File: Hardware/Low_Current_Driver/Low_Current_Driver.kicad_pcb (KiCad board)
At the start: 4 copper layers, 0 parts

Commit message: Checkpoint before channel-replication refactor
Snapshot of schematic/PCB work-in-progress prior to restructuring
Channel_Outputs into a reusable hierarchical channel sheet for
replicate-layout. Adds DPST relay footprint.

Co-Authored-By: Claude Opus 4.8 <noreply@anthropic.com>
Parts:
- added A1: Arduino_Nano_Every, Module:Arduino_Nano, F.Cu at (187.5, 108.2)
- added C10: 10n, Capacitor_SMD:C_0603_1608Metric_Pad1.08x0.95mm_HandSolder, F.Cu at (154.7, 98.2)
- added C11: 47u, Capacitor_SMD:C_1210_3225Metric_Pad1.33x2.70mm_HandSolder, F.Cu at (154.9, 76.2)
- added C12: 47u, Capacitor_SMD:C_1210_3225Metric_Pad1.33x2.70mm_HandSolder, F.Cu at (155.9, 86.2)
- added C13: 47u, Capacitor_SMD:C_1210_3225Metric_Pad1.33x2.70mm_HandSolder, F.Cu at (161.9, 97.3)
- added C14: 100n, Capacitor_SMD:C_0603_1608Metric_Pad1.08x0.95mm_HandSolder, F.Cu at (196.3, 70.2)
- added C15: 100n, Capacitor_SMD:C_0603_1608Metric_Pad1.08x0.95mm_HandSolder, F.Cu at (223.3, 78.2)
- added C16: 100n, Capacitor_SMD:C_0603_1608Metric_Pad1.08x0.95mm_HandSolder, F.Cu at (214.4, 88.2)
- added C17: 100n, Capacitor_SMD:C_0603_1608Metric_Pad1.08x0.95mm_HandSolder, F.Cu at (219.8, 89.7)
- added C18: 100n, Capacitor_SMD:C_0603_1608Metric_Pad1.08x0.95mm_HandSolder, F.Cu at (212.3, 103.2)
- added C21: 1u, Capacitor_SMD:C_0603_1608Metric_Pad1.08x0.95mm_HandSolder, F.Cu at (223.4, 80.2)
- added C22: 1u, Capacitor_SMD:C_0603_1608Metric_Pad1.08x0.95mm_HandSolder, F.Cu at (214.4, 90.7)
- added C23: 47u, Capacitor_SMD:C_1210_3225Metric_Pad1.33x2.70mm_HandSolder, F.Cu at (203.2, 80.6)
- added C24: 1u, Capacitor_SMD:C_0603_1608Metric_Pad1.08x0.95mm_HandSolder, F.Cu at (219.8, 92.2)
- added C25: 1u, Capacitor_SMD:C_0603_1608Metric_Pad1.08x0.95mm_HandSolder, F.Cu at (212.1, 100.6)
- added C28: 10u, Capacitor_SMD:C_1206_3216Metric_Pad1.33x1.80mm_HandSolder, F.Cu at (203.2, 76.8)
- added C29: 10n, Capacitor_SMD:C_0603_1608Metric_Pad1.08x0.95mm_HandSolder, F.Cu at (209.8, 89.1)
- added C30: 100n, Capacitor_SMD:C_0603_1608Metric_Pad1.08x0.95mm_HandSolder, F.Cu at (209.8, 91.2)
- added C34: 100n, Capacitor_SMD:C_0603_1608Metric_Pad1.08x0.95mm_HandSolder, F.Cu at (223.9, 96.2)
- added C35: 100n, Capacitor_SMD:C_0603_1608Metric_Pad1.08x0.95mm_HandSolder, F.Cu at (228.4, 84.7)
- added C37: 100n, Capacitor_SMD:C_0603_1608Metric_Pad1.08x0.95mm_HandSolder, F.Cu at (253.9, 93.7)
- added C38: 100n, Capacitor_SMD:C_0603_1608Metric_Pad1.08x0.95mm_HandSolder, F.Cu at (246.4, 102.7)
- added C39: 100n, Capacitor_SMD:C_0603_1608Metric_Pad1.08x0.95mm_HandSolder, F.Cu at (268.0, 87.1)
- added C4: 10u, Capacitor_SMD:C_1206_3216Metric_Pad1.33x1.80mm_HandSolder, F.Cu at (144.7, 73.7)
- added C40: 100n, Capacitor_SMD:C_0603_1608Metric_Pad1.08x0.95mm_HandSolder, F.Cu at (268.0, 89.6)
- added C49: 1u, Capacitor_SMD:C_0603_1608Metric_Pad1.08x0.95mm_HandSolder, F.Cu at (243.9, 99.7)
- added C5: 10u, Capacitor_SMD:C_1206_3216Metric_Pad1.33x1.80mm_HandSolder, F.Cu at (144.7, 87.7)
- added C50: 1u, Capacitor_SMD:C_0603_1608Metric_Pad1.08x0.95mm_HandSolder, F.Cu at (240.8, 75.9)
- added C52: 1u, Capacitor_SMD:C_0603_1608Metric_Pad1.08x0.95mm_HandSolder, F.Cu at (246.9, 94.2)
- added C53: 1u, Capacitor_SMD:C_0603_1608Metric_Pad1.08x0.95mm_HandSolder, F.Cu at (240.8, 80.9)
- added C54: 4.7u, Capacitor_SMD:C_0603_1608Metric_Pad1.08x0.95mm_HandSolder, F.Cu at (238.9, 102.7)
- added C55: 4.7u, Capacitor_SMD:C_0603_1608Metric_Pad1.08x0.95mm_HandSolder, F.Cu at (245.1, 65.8)
- added C6: 10u, Capacitor_SMD:C_1206_3216Metric_Pad1.33x1.80mm_HandSolder, F.Cu at (145.9, 103.2)
- added C7: 1u, Capacitor_SMD:C_0603_1608Metric_Pad1.08x0.95mm_HandSolder, F.Cu at (144.7, 79.2)
- added C8: 1u, Capacitor_SMD:C_0603_1608Metric_Pad1.08x0.95mm_HandSolder, F.Cu at (149.4, 83.2)
- added C9: 1u, Capacitor_SMD:C_0603_1608Metric_Pad1.08x0.95mm_HandSolder, F.Cu at (144.9, 97.3)
- added J1: Conn_01x02_Socket, Connector_Molex:Molex_Micro-Fit_3.0_43650-0215_1x02_P3.00mm_Vertical, F.Cu at (307.4, 84.3)
- added J2: Conn_01x02_Socket, Connector_Molex:Molex_Micro-Fit_3.0_43650-0215_1x02_P3.00mm_Vertical, F.Cu at (307.4, 92.1)
- added J3: Screw_Terminal_01x04, TerminalBlock_Phoenix:TerminalBlock_Phoenix_MKDS-1,5-4-5.08_1x04_P5.08mm_Horizontal, F.Cu at (110.2, 80.0)
- added NT1: Net-Tie_3, NetTie:NetTie-3_SMD_Pad2.0mm, F.Cu at (214.4, 47.6)
- added R13: 549k, Resistor_SMD:R_0603_1608Metric_Pad0.98x0.95mm_HandSolder, F.Cu at (157.9, 98.2)
- added R14: 102k, Resistor_SMD:R_0603_1608Metric_Pad0.98x0.95mm_HandSolder, F.Cu at (157.9, 94.1)
- added R18: 10k, Resistor_SMD:R_0603_1608Metric_Pad0.98x0.95mm_HandSolder, F.Cu at (200.9, 98.2)
- added R19: 10k, Resistor_SMD:R_0603_1608Metric_Pad0.98x0.95mm_HandSolder, F.Cu at (202.9, 98.2)
- added R20: 10k, Resistor_SMD:R_0603_1608Metric_Pad0.98x0.95mm_HandSolder, F.Cu at (221.4, 100.3)
- added R21: 10k, Resistor_SMD:R_0603_1608Metric_Pad0.98x0.95mm_HandSolder, F.Cu at (208.4, 93.8)
- added R22: 10k, Resistor_SMD:R_0603_1608Metric_Pad0.98x0.95mm_HandSolder, F.Cu at (210.4, 94.2)
- added R23: 10k, Resistor_SMD:R_0603_1608Metric_Pad0.98x0.95mm_HandSolder, F.Cu at (225.4, 88.7)
- added R24: 10k, Resistor_SMD:R_0603_1608Metric_Pad0.98x0.95mm_HandSolder, F.Cu at (211.4, 82.2)
- added R25: 10k, Resistor_SMD:R_0603_1608Metric_Pad0.98x0.95mm_HandSolder, F.Cu at (213.4, 82.2)
- added R29: 10k, Resistor_SMD:R_0603_1608Metric_Pad0.98x0.95mm_HandSolder, F.Cu at (221.4, 96.3)
- added R30: 10k, Resistor_SMD:R_0603_1608Metric_Pad0.98x0.95mm_HandSolder, F.Cu at (225.4, 84.7)
- added R32: 1k, Resistor_SMD:R_0603_1608Metric_Pad0.98x0.95mm_HandSolder, F.Cu at (240.4, 96.7)
- added R33: 1k, Resistor_SMD:R_0603_1608Metric_Pad0.98x0.95mm_HandSolder, F.Cu at (245.1, 70.9)
- added R35: 1k, Resistor_SMD:R_0603_1608Metric_Pad0.98x0.95mm_HandSolder, F.Cu at (244.9, 96.7)
- added R36: 1k, Resistor_SMD:R_0603_1608Metric_Pad0.98x0.95mm_HandSolder, F.Cu at (245.1, 75.9)
- added R38: 1k, Resistor_SMD:R_0603_1608Metric_Pad0.98x0.95mm_HandSolder, F.Cu at (257.4, 102.1)
- added R39: 249, Resistor_SMD:R_0603_1608Metric_Pad0.98x0.95mm_HandSolder, F.Cu at (249.5, 103.7)
- added R40: 1k, Resistor_SMD:R_0603_1608Metric_Pad0.98x0.95mm_HandSolder, F.Cu at (249.5, 63.3)
- added R41: 249, Resistor_SMD:R_0603_1608Metric_Pad0.98x0.95mm_HandSolder, F.Cu at (249.5, 65.8)
- added R44: 1k, Resistor_SMD:R_0603_1608Metric_Pad0.98x0.95mm_HandSolder, F.Cu at (257.4, 98.0)
- added R45: 1k, Resistor_SMD:R_0603_1608Metric_Pad0.98x0.95mm_HandSolder, F.Cu at (253.4, 103.7)
- added R46: 1k, Resistor_SMD:R_0603_1608Metric_Pad0.98x0.95mm_HandSolder, F.Cu at (249.5, 73.4)
- added R47: 1k, Resistor_SMD:R_0603_1608Metric_Pad0.98x0.95mm_HandSolder, F.Cu at (249.5, 75.9)
- added SW1: SW_DPST, fieldZero:DPST_RA83231100, F.Cu at (129.3, 87.6)
- added TP1: TestPoint_Probe, TestPoint:TestPoint_Pad_D1.0mm, F.Cu at (134.4, 77.6)
- added TP12: TestPoint_Probe, TestPoint:TestPoint_Pad_D1.0mm, F.Cu at (154.4, 90.2)
- added TP13: TestPoint_Probe, TestPoint:TestPoint_Pad_D1.0mm, F.Cu at (154.9, 102.7)
- added TP14: TestPoint_Probe, TestPoint:TestPoint_Pad_D1.0mm, F.Cu at (154.9, 80.2)
- added TP15: TestPoint_Probe, TestPoint:TestPoint_Pad_D1.0mm, F.Cu at (203.9, 68.1)
- added TP16: TestPoint_Probe, TestPoint:TestPoint_Pad_D1.0mm, F.Cu at (203.9, 71.2)
- added TP17: TestPoint_Probe, TestPoint:TestPoint_Pad_D1.0mm, F.Cu at (218.8, 124.7)
- added TP18: TestPoint_Probe, TestPoint:TestPoint_Pad_D1.0mm, F.Cu at (221.9, 118.6)
- added TP19: TestPoint_Probe, TestPoint:TestPoint_Pad_D1.0mm, F.Cu at (221.9, 121.7)
- added TP2: TestPoint_Probe, TestPoint:TestPoint_Pad_D1.0mm, F.Cu at (134.4, 97.6)
- added TP20: TestPoint_Probe, TestPoint:TestPoint_Pad_D1.0mm, F.Cu at (221.9, 124.7)
- added TP21: TestPoint_Probe, TestPoint:TestPoint_Pad_D1.0mm, F.Cu at (224.9, 118.6)
- added TP23: TestPoint_Probe, TestPoint:TestPoint_Pad_D1.0mm, F.Cu at (83.4, 53.5)
- added TP24: TestPoint_Probe, TestPoint:TestPoint_Pad_D1.0mm, F.Cu at (83.4, 56.6)
- added TP25: TestPoint_Probe, TestPoint:TestPoint_Pad_D1.0mm, F.Cu at (83.4, 59.6)
- added TP26: TestPoint_Probe, TestPoint:TestPoint_Pad_D1.0mm, F.Cu at (83.4, 62.7)
- added TP27: TestPoint_Probe, TestPoint:TestPoint_Pad_D1.0mm, F.Cu at (86.5, 53.5)
- added TP28: TestPoint_Probe, TestPoint:TestPoint_Pad_D1.0mm, F.Cu at (86.5, 56.6)
- added TP30: TestPoint_Probe, TestPoint:TestPoint_Pad_D1.0mm, F.Cu at (133.9, 115.7)
- added TP31: TestPoint_Probe, TestPoint:TestPoint_Pad_D1.0mm, F.Cu at (264.4, 125.6)
- added TP32: TestPoint_Probe, TestPoint:TestPoint_Pad_D1.0mm, F.Cu at (253.2, 79.8)
- added TP33: TestPoint_Probe, TestPoint:TestPoint_Pad_D1.0mm, F.Cu at (267.4, 125.6)
- added TP34: TestPoint_Probe, TestPoint:TestPoint_Pad_D1.0mm, F.Cu at (267.4, 128.7)
- added TP35: TestPoint_Probe, TestPoint:TestPoint_Pad_D1.0mm, F.Cu at (259.3, 76.8)
- added TP36: TestPoint_Probe, TestPoint:TestPoint_Pad_D1.0mm, F.Cu at (259.3, 79.8)
- added TP41: TestPoint_Probe, TestPoint:TestPoint_Pad_D1.0mm, F.Cu at (233.4, 95.6)
- added TP42: TestPoint_Probe, TestPoint:TestPoint_Pad_D1.0mm, F.Cu at (233.4, 98.7)
- added TP43: TestPoint_Probe, TestPoint:TestPoint_Pad_D1.0mm, F.Cu at (233.4, 84.1)
- added TP44: TestPoint_Probe, TestPoint:TestPoint_Pad_D1.0mm, F.Cu at (233.4, 87.2)
- added TP47: TestPoint_Probe, TestPoint:TestPoint_Pad_D1.0mm, F.Cu at (228.0, 124.7)
- added U10: OPA2210, Package_SO:SOIC-8_3.9x4.9mm_P1.27mm, F.Cu at (218.4, 84.7)
- added U12: OPA2210, Package_SO:SOIC-8_3.9x4.9mm_P1.27mm, F.Cu at (250.9, 98.2)
- added U13: OPA2210, Package_SO:SOIC-8_3.9x4.9mm_P1.27mm, F.Cu at (255.9, 72.0)
- added U4: TPS7A470x, Package_DFN_QFN:QFN-20-1EP_5x5mm_P0.65mm_EP3.35x3.35mm_ThermalVias, F.Cu at (149.4, 77.6)
- added U5: TPS7A470x, Package_DFN_QFN:QFN-20-1EP_5x5mm_P0.65mm_EP3.35x3.35mm_ThermalVias, F.Cu at (149.6, 87.4)
- added U6: TPS7A33, Package_DFN_QFN:QFN-20-1EP_5x5mm_P0.65mm_EP3.35x3.35mm_ThermalVias, F.Cu at (149.4, 97.6)
- added U7: LTC6655-2.5, Package_LCC:Analog_LCC-8_5x5mm_P1.27mm, F.Cu at (196.6, 78.9)
- added U8: DAC8814, Package_SO:SSOP-28_5.3x10.2mm_P0.65mm, F.Cu at (201.9, 90.2)
- added U9: OPA2210, Package_SO:SOIC-8_3.9x4.9mm_P1.27mm, F.Cu at (215.9, 96.2)
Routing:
- net -9V: track 0.00 -> 16.3 mm
- net /Power/-9V_raw: track 0.00 -> 15.9 mm
- net /Power/+9V_raw: track 0.00 -> 15.6 mm
- net +9V: track 0.00 -> 10.8 mm

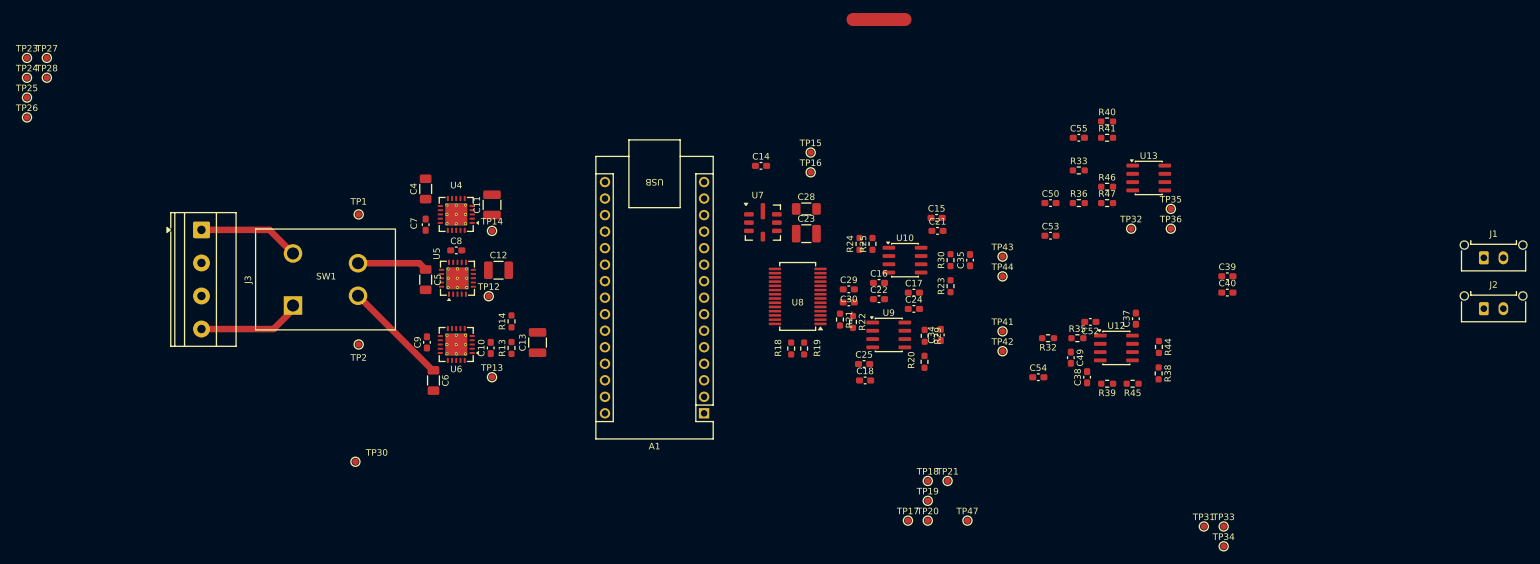
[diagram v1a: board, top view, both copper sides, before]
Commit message: Replicate coil drive channel via native multichannel sheets
Root schematic now instantiates Channel_Outputs.kicad_sch twice as
Coil_Drive_A / Coil_Drive_B, with DAC_OPA.kicad_sch added as a sub-sheet
of DAC.kicad_sch (also instantiated twice). PCB relaid out to match.

Also drops the abandoned ESP32-S3 leftovers (footprint file and the
sym-lib-table entry pointing at an absolute path), removes the stale
Low_Current_Driver-cache legacy lib entry, and adds the STEP models
referenced by the board under 3DModels/.

Co-Authored-By: Claude Opus 4.8 <noreply@anthropic.com>
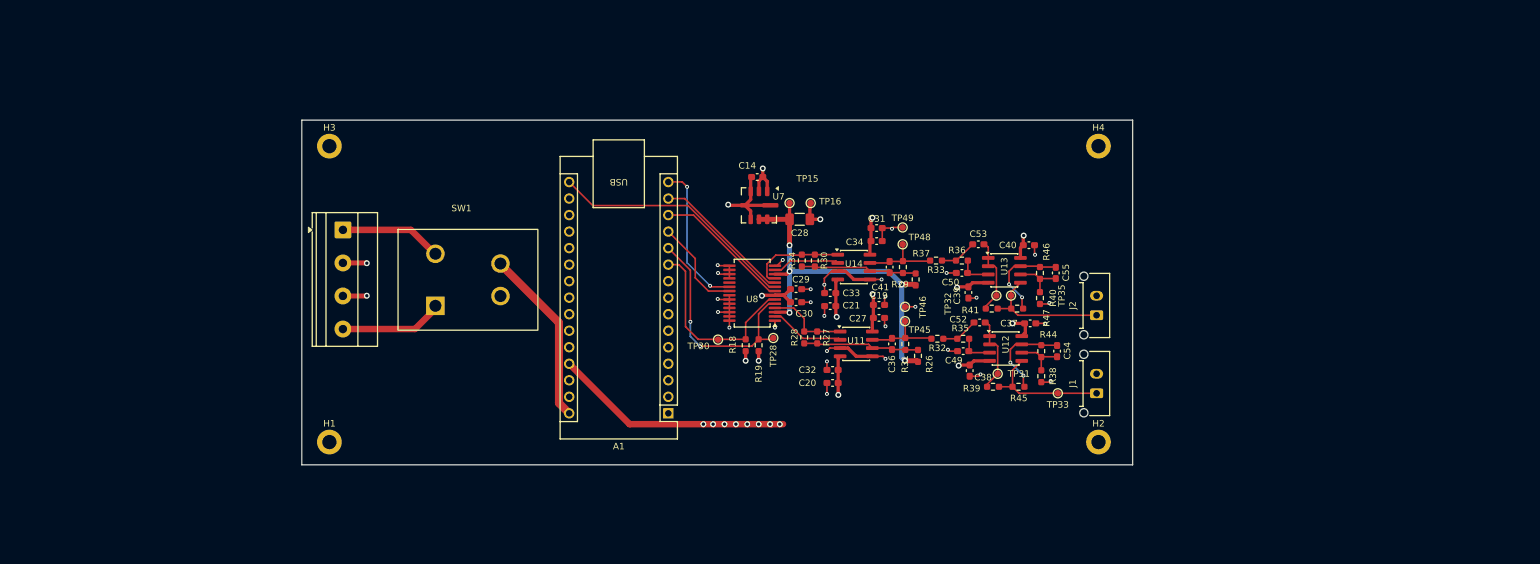
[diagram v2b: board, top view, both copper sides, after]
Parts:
- removed C10: 10n, Capacitor_SMD:C_0603_1608Metric_Pad1.08x0.95mm_HandSolder
- removed C11, C12, C13, C23: 47u, Capacitor_SMD:C_1210_3225Metric_Pad1.33x2.70mm_HandSolder
- removed C15, C16, C17, C18, C35: 100n, Capacitor_SMD:C_0603_1608Metric_Pad1.08x0.95mm_HandSolder
- removed C22, C24, C25, C7, C8, C9: 1u, Capacitor_SMD:C_0603_1608Metric_Pad1.08x0.95mm_HandSolder
- removed C4, C5, C6: 10u, Capacitor_SMD:C_1206_3216Metric_Pad1.33x1.80mm_HandSolder
- removed NT1: Net-Tie_3, NetTie:NetTie-3_SMD_Pad2.0mm
- removed R13: 549k, Resistor_SMD:R_0603_1608Metric_Pad0.98x0.95mm_HandSolder
- removed R14: 102k, Resistor_SMD:R_0603_1608Metric_Pad0.98x0.95mm_HandSolder
- removed R20, R21, R22, R23, R24, R25: 10k, Resistor_SMD:R_0603_1608Metric_Pad0.98x0.95mm_HandSolder
- removed TP1, TP12, TP13, TP14, TP17, TP18, TP19, TP2, TP20, TP21, TP23, TP24, TP25, TP26, TP27, TP34, TP36, TP41, TP42, TP43, TP44, TP47: TestPoint_Probe, TestPoint:TestPoint_Pad_D1.0mm
- removed U10, U9: OPA2210, Package_SO:SOIC-8_3.9x4.9mm_P1.27mm
- removed U4, U5: TPS7A470x, Package_DFN_QFN:QFN-20-1EP_5x5mm_P0.65mm_EP3.35x3.35mm_ThermalVias
- removed U6: TPS7A33, Package_DFN_QFN:QFN-20-1EP_5x5mm_P0.65mm_EP3.35x3.35mm_ThermalVias
- added C19: 100n, Capacitor_SMD:C_0603_1608Metric_Pad1.08x0.95mm_HandSolder, F.Cu at (214.4, 91.5)
- added C20: 100n, Capacitor_SMD:C_0603_1608Metric_Pad1.08x0.95mm_HandSolder, F.Cu at (207.3, 103.5)
- added C27: 1u, Capacitor_SMD:C_0603_1608Metric_Pad1.08x0.95mm_HandSolder, F.Cu at (214.4, 93.5)
- added C31: 100n, Capacitor_SMD:C_0603_1608Metric_Pad1.08x0.95mm_HandSolder, F.Cu at (214.0, 79.7)
- added C32: 1u, Capacitor_SMD:C_0603_1608Metric_Pad1.08x0.95mm_HandSolder, F.Cu at (207.3, 101.5)
- added C33: 1u, Capacitor_SMD:C_0603_1608Metric_Pad1.08x0.95mm_HandSolder, F.Cu at (206.9, 89.7)
- added C36: 100n, Capacitor_SMD:C_0603_1608Metric_Pad1.08x0.95mm_HandSolder, F.Cu at (216.4, 97.5)
- added C41: 100n, Capacitor_SMD:C_0603_1608Metric_Pad1.08x0.95mm_HandSolder, F.Cu at (216.0, 85.7)
- added H1: MountingHole_Pad, MountingHole:MountingHole_2.2mm_M2_DIN965_Pad, F.Cu at (129.9, 112.6)
- added H2: MountingHole_Pad, MountingHole:MountingHole_2.2mm_M2_DIN965_Pad, F.Cu at (248.2, 112.6)
- added H3: MountingHole_Pad, MountingHole:MountingHole_2.2mm_M2_DIN965_Pad, F.Cu at (129.9, 67.1)
- added H4: MountingHole_Pad, MountingHole:MountingHole_2.2mm_M2_DIN965_Pad, F.Cu at (248.2, 67.1)
- added R26: 10k, Resistor_SMD:R_0603_1608Metric_Pad0.98x0.95mm_HandSolder, F.Cu at (220.4, 99.4)
- added R27: 10k, Resistor_SMD:R_0603_1608Metric_Pad0.98x0.95mm_HandSolder, F.Cu at (204.9, 96.5)
- added R28: 10k, Resistor_SMD:R_0603_1608Metric_Pad0.98x0.95mm_HandSolder, F.Cu at (202.9, 96.5)
- added R31: 10k, Resistor_SMD:R_0603_1608Metric_Pad0.98x0.95mm_HandSolder, F.Cu at (218.4, 97.5)
- added R34: 10k, Resistor_SMD:R_0603_1608Metric_Pad0.98x0.95mm_HandSolder, F.Cu at (202.5, 84.7)
- added R37: 10k, Resistor_SMD:R_0603_1608Metric_Pad0.98x0.95mm_HandSolder, F.Cu at (218.1, 85.7)
- added TP45: TestPoint_Probe, TestPoint:TestPoint_Pad_D1.0mm, F.Cu at (218.4, 94.0)
- added TP46: TestPoint_Probe, TestPoint:TestPoint_Pad_D1.0mm, F.Cu at (218.4, 91.8)
- added TP48: TestPoint_Probe, TestPoint:TestPoint_Pad_D1.0mm, F.Cu at (218.0, 82.2)
- added TP49: TestPoint_Probe, TestPoint:TestPoint_Pad_D1.0mm, F.Cu at (218.0, 79.6)
- added U11: OPA2210, Package_SO:SOIC-8_3.9x4.9mm_P1.27mm, F.Cu at (210.9, 97.5)
- added U14: OPA2210, Package_SO:SOIC-8_3.9x4.9mm_P1.27mm, F.Cu at (210.5, 85.7)
- A1: value Arduino_Nano_Every -> Arduino_Nano_R4
- C21: value 1u -> 100n
- C34: value 100n -> 1u
- R38, R40, R44, R45, R46, R47: value 1k -> 249
- moved TP28 118.7 mm to (198.2, 96.6)
- moved J1 63.1 mm to (247.9, 105.1), turned to 90 degrees
- moved J2 59.5 mm to (247.9, 93.1), turned to 90 degrees
- moved TP30 58.8 mm to (189.7, 96.9)
- moved C39 39.9 mm to (228.2, 89.6), turned to 90 degrees
- moved TP31 39.4 mm to (232.7, 102.1)
- moved TP33 32.7 mm to (241.9, 105.1)
- moved R41 31.7 mm to (231.7, 92.1), turned to 180 degrees
- moved C40 31.4 mm to (237.4, 82.3)
- moved R40 29.0 mm to (239.2, 90.5), turned to -90 degrees
- moved TP35 28.0 mm to (234.7, 90.1)
- moved U13 26.4 mm to (233.7, 86.2)
- moved R33 26.0 mm to (223.2, 84.7), turned to 180 degrees
- moved TP32 23.1 mm to (232.4, 90.1)
- moved SW1 21.9 mm to (151.2, 87.7)
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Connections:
- net /Channel_Outputs/U12Bin- renamed /Coil_Drive_A/HCP_FB
- net /Channel_Outputs/U12Bout renamed /Coil_Drive_A/HCP_Out
- net /Channel_Outputs/U13Bin- renamed /Coil_Drive_B/HCP_FB
- net /Channel_Outputs/U13Bout renamed /Coil_Drive_B/HCP_Out
- net /Power/+9V_raw renamed Net-(J3-Pin_1)
- net /Power/-9V_raw renamed Net-(J3-Pin_4)
- A1 pad 29: GNDD -> GND
- A1 pad 4: GNDD -> GND
- C14 pad 1: +7V5 -> +5VD
- C21 pad 1: +7V5 -> -9V
- C29 pad 1: +5V -> +5VD
- C30 pad 1: +5V -> +5VD
- C34 pad 1: Net-(U9B--) -> +9V
- C34 pad 2: /DAC/Vout_A -> GND
- C37 pad 1: +7V5 -> +9V
- C38 pad 2: -7V5 -> -9V
- C39 pad 1: +7V5 -> GND
- C39 pad 2: GND -> -9V
- C40 pad 1: GND -> +9V
- C40 pad 2: -7V5 -> GND
- J1 pad 1: /Channel_Outputs/U13Bin+ -> /Coil_Drive_A/Iin_coil
- J2 pad 1: /Channel_Outputs/U12Bin+ -> /Coil_Drive_B/Iin_coil
- R29 pad 1: Net-(U9B--) -> /DAC/Vref_2.5V
- R29 pad 2: /DAC/Vout_A -> Net-(U14B--)
- R30 pad 1: Net-(U10B--) -> /DAC/DAC_Buffer_B/Rfb
- R30 pad 2: /DAC/Vout_B -> Net-(U14B--)
- R32 pad 2: /DAC/Vout_A -> /Coil_Drive_A/Vout_dac
- R33 pad 2: /DAC/Vout_B -> /Coil_Drive_B/Vout_dac
- R39 pad 1: /Channel_Outputs/U12Bin+ -> /Coil_Drive_A/Iin_coil
- R41 pad 1: /Channel_Outputs/U13Bin+ -> /Coil_Drive_B/Iin_coil
- R45 pad 2: /Channel_Outputs/U12Bin+ -> /Coil_Drive_A/Iin_coil
- R47 pad 2: /Channel_Outputs/U13Bin+ -> /Coil_Drive_B/Iin_coil
- TP33 pad 1: /Channel_Outputs/U12Bin+ -> /Coil_Drive_A/Iin_coil
- TP35 pad 1: /Channel_Outputs/U13Bin+ -> /Coil_Drive_B/Iin_coil
- U12 pad 4: -7V5 -> -9V
- U12 pad 5: /Channel_Outputs/U12Bin+ -> /Coil_Drive_A/Iin_coil
- U12 pad 8: +7V5 -> +9V
- U13 pad 4: -7V5 -> -9V
- U13 pad 5: /Channel_Outputs/U13Bin+ -> /Coil_Drive_B/Iin_coil
- U13 pad 8: +7V5 -> +9V
- U7 pad 1: +7V5 -> +5VD
- U7 pad 2: +7V5 -> +5VD
- U7 pad 6: Net-(U7-Vout_S) -> /DAC/Vref_2.5V
- U8 pad 11: /DAC/Vout_B_DAC -> /DAC/DAC_Buffer_B/Rfb
- U8 pad 13: /DAC/Iout_B -> /DAC/DAC_Buffer_B/Iin
- U8 pad 16: unconnected-(U8-Iout_C-Pad16) -> GND
- U8 pad 17: /DAC/Vref_2.5V -> GND
- U8 pad 18: unconnected-(U8-Rfb_C-Pad18) -> GND
- U8 pad 2: /DAC/I_outA -> /DAC/DAC_Buffer_A/Iin
- U8 pad 25: unconnected-(U8-Rfb_D-Pad25) -> GND
- U8 pad 26: /DAC/Vref_2.5V -> GND
- U8 pad 27: unconnected-(U8-Iout_D-Pad27) -> GND
- U8 pad 4: /DAC/Vout_A_DAC -> /DAC/DAC_Buffer_A/Rfb
- U8 pad 7: +5V -> +5VD
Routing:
- net +9V: track 10.8 -> 140.9 mm, vias 0 -> 4
- net -9V: track 16.3 -> 113.2 mm, vias 0 -> 4
- net GND: track 0.00 -> 93.3 mm, vias 0 -> 32
- net /DAC/Vref_2.5V: track 0.00 -> 60.6 mm, vias 0 -> 5
- net +5VD: track 0.00 -> 53.6 mm, vias 0 -> 12
- net /DAC/CLK: track 0.00 -> 38.3 mm
- net /DAC/MSB: track 0.00 -> 35.9 mm, vias 0 -> 2
- net /DAC/~{RS}: track 0.00 -> 30.2 mm
- net /DAC/SDO: track 0.00 -> 22.9 mm, vias 0 -> 2
- net /DAC/SDI: track 0.00 -> 21.7 mm
- net /DAC/~{CS}: track 0.00 -> 21.2 mm
- net /Coil_Drive_B/Iin_coil: track 0.00 -> 20.2 mm
- net /Coil_Drive_A/Iin_coil: track 0.00 -> 20.0 mm
- net Net-(U14B--): track 0.00 -> 17.9 mm
- net Net-(U11B--): track 0.00 -> 17.9 mm
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- added copper zone on In2.Cu, net +5VD
- added copper zone on In2.Cu, net +9V
- added copper zone on In2.Cu, net -9V
- added copper zone on In1.Cu, net GND
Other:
- board outline added: 127.8 x 53 mm
- rule solder_mask_min_width: 0.25 -> 0.1

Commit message: Add fab1 package and update docs to as-built for first prototype
- Add fab1.zip + gerbers/drills (4-layer, 127.75x53mm) for JLC bare-board order
- Rewrite context.md PCB section to as-built: external raw ±9V via J3→SW1,
  no on-board LDOs/battery-mgmt; record removed Power/Battery_Management/
  Mounting_Holes sheets and honest ERC state (2 residual errors on DAC8814
  unused C/D outputs, benign)
- Add "Fabrication — first prototype" section: board stack, $25 JLC NRE fee,
  DRC clean, DigiKey BOM verified Active 2026-07-23
- Finalize channel-replication refactor edits (DAC/DAC_OPA/Channel_Outputs)
- Remove stale DRC violations report

Co-Authored-By: Claude Opus 4.8 <noreply@anthropic.com>
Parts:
- moved Coil 8.30 mm to (242.4, 93.1)
- renumbered TP15 to 2.5V, TP33 to Coil, TP35 to Coil, TP45 to DAC1, TP48 to DAC2, TP46 to GND, TP16 to GND, TP49 to GND, TP31 to HCP, TP32 to HCP, TP28 to MSB, TP30 to RS
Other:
- board text added: "Differential Low Current Driver Designer: Kayzer Date: 23/07/2026 Contact: s4962116@student.uq.edu.au Version: v010"
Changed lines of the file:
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@@
 			(plot_on_all_layers_selection 0x00000000_00000000_00000000_00000000)
 			(disableapertmacros no)
-			(usegerberextensions no)
-			(usegerberattributes yes)
+			(usegerberextensions yes)
+			(usegerberattributes no)
 			(usegerberadvancedattributes no)
 			(creategerberjobfile no)
@@
 			(plotframeref no)
 			(mode 1)
-			(useauxorigin yes)
+			(useauxorigin no)
 			(pdf_front_fp_property_popups yes)
 			(pdf_back_fp_property_popups yes)
@@
 			(sketchdnponfab yes)
 			(crossoutdnponfab yes)
-			(subtractmaskfromsilk no)
+			(subtractmaskfromsilk yes)
 			(outputformat 1)
 			(mirror no)
 			(drillshape 0)
 			(scaleselection 1)
-			(outputdirectory "gerber/")
+			(outputdirectory "fab/")
 		)
 	)
@@
 		(descr "SMD pad as test Point, diameter 1.0mm")
 		(tags "test point SMD pad")
-		(property "Reference" "TP31"
-			(at 3.25 0 0)
+		(property "Reference" "HCP"
+			(at -2.25 -0.25 90)
 			(layer "F.SilkS")
 			(effects
@@
 		(tags "capacitor handsolder")
 		(property "Reference" "C38"
-			(at -1.03 2.05 0)
+			(at -0.48 -2.45 0)
 			(layer "F.SilkS")
 			(effects
@@
 		(descr "SMD pad as test Point, diameter 1.0mm")
 		(tags "test point SMD pad")
-		(property "Reference" "TP46"
-			(at 2.75 0.05 90)
+		(property "Reference" "GND"
+			(at 2.5 -0.95 180)
 			(layer "F.SilkS")
 			(effects
@@
 		(descr "SMD pad as test Point, diameter 1.0mm")
 		(tags "test point SMD pad")
-		(property "Reference" "TP16"
-			(at 3 -0.25 0)
+		(property "Reference" "GND"
+			(at 1.25 -2 0)
 			(layer "F.SilkS")
 			(effects
@@
 		(tags "resistor handsolder")
 		(property "Reference" "R39"
-			(at 3.2875 -0.25 0)
+			(at -0.2125 -1.75 0)
 			(layer "F.SilkS")
 			(effects
@@
 		(descr "SMD pad as test Point, diameter 1.0mm")
 		(tags "test point SMD pad")
-		(property "Reference" "TP28"
+		(property "Reference" "MSB"
 			(at 0 2.75 90)
 			(layer "F.SilkS")
@@
 		(descr "SMD pad as test Point, diameter 1.0mm")
 		(tags "test point SMD pad")
-		(property "Reference" "TP49"
-			(at 0 -1.448 0)
+		(property "Reference" "GND"
+			(at 0 -1.75 0)
 			(layer "F.SilkS")
 			(effects
@@
 		(tags "resistor handsolder")
 		(property "Reference" "R37"
-			(at 2.095 2.8225 180)
+			(at 1.345 2.0725 180)
 			(layer "F.SilkS")
 			(effects
@@
 		(descr "SMD pad as test Point, diameter 1.0mm")
 		(tags "test point SMD pad")
-		(property "Reference" "TP45"
-			(at 2.25 1.3375 0)
+		(property "Reference" "DAC1"
+			(at 2.75 -0.6625 0)
 			(layer "F.SilkS")
 			(effects
@@
 		(descr "SMD pad as test Point, diameter 1.0mm")
 		(tags "test point SMD pad")
-		(property "Reference" "TP15"
-			(at 2.75 -3.75 0)
+		(property "Reference" "2.5V"
+			(at 0.5 -2 0)
 			(layer "F.SilkS")
 			(effects
@@
 		(descr "SMD pad as test Point, diameter 1.0mm")
 		(tags "test point SMD pad")
-		(property "Reference" "TP33"
+		(property "Reference" "Coil"
 			(at 0 1.75 180)
 			(layer "F.SilkS")
@@
 		(descr "SMD pad as test Point, diameter 1.0mm")
 		(tags "test point SMD pad")
-		(property "Reference" "TP32"
-			(at -7.4364 1.2423 90)
+		(property "Reference" "HCP"
+			(at -1.8 -0.23 90)
 			(layer "F.SilkS")
 			(effects
@@
 		(descr "SMD pad as test Point, diameter 1.0mm")
 		(tags "test point SMD pad")
-		(property "Reference" "TP48"
+		(property "Reference" "DAC2"
 			(at 2.6125 -1.095 0)
 			(layer "F.SilkS")
@@
 	(footprint "TestPoint:TestPoint_Pad_D1.0mm"
 		(layer "F.Cu")
-		(at 234.7 90.1)
+		(at 242.44 93.1)
 		(descr "SMD pad as test Point, diameter 1.0mm")
 		(tags "test point SMD pad")
-		(property "Reference" "TP35"
-			(at 7.8 0 90)
+		(property "Reference" "Coil"
+			(at -0.04 1.77 180)
 			(layer "F.SilkS")
 			(effects
@@
 		(tags "lcc smt")
 		(property "Reference" "U7"
-			(at -1.35 -3.02 180)
+			(at -1.85 4.5425 180)
 			(layer "F.SilkS")
 			(effects
@@
 		(descr "SMD pad as test Point, diameter 1.0mm")
 		(tags "test point SMD pad")
-		(property "Reference" "TP30"
-			(at -3 1 0)
+		(property "Reference" "RS"
+			(at -1.25 -1.75 0)
 			(layer "F.SilkS")
 			(effects
@@
 		(layer "Edge.Cuts")
 	)
+	(gr_text "Differential Low Current Driver\nDesigner: Kayzer\nDate: 23/07/2026\nContact: s4962116@student.uq.edu.au\nVersion: v010"
+		(at 135.15 114.37 0)
+		(layer "F.SilkS")
+		(effects
+			(font
+				(size 1 1)
+				(thickness 0.15)
+			)
+			(justify left bottom)
+		)
+	)
 	(segment
